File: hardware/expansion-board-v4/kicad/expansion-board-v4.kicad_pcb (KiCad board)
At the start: 6 copper layers, 100 x 62 mm, 176 parts, among them J1 PinHeader_2x20_P2.54mm_Vertic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, J2 U.FL_Hirose_U.FL-R-SMT-1_Vert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, J4 USB_C_Receptacle_HRO_TYPE-C-3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, J5 U.FL_Hirose_U.FL-R-SMT-1_Vert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, J6 U.FL_Hirose_U.FL-R-SMT-1_Vert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, J7 U.FL_Hirose_U.FL-R-SMT-1_Vert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, J8 U.FL_Hirose_U.FL-R-SMT-1_Vert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, J9 MX1.25WT-2P, Q2 SOT-23, Q3 SOT-23, Q4 SOT-23, Q5 SOT-23, SW2 SolderJumper-2_P1.3mm_Open_Pa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, U1 SOT-23-5, U10 QFN-48-1EP_7x7mm_P0.5mm_EP5.1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, U11 DFN-8-1EP_2x2mm_P0.5mm_EP0.86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, U12 SOT-363_SC-70-6, U13 AD8319_LFCSP-8-EP, U14 MSOP-8_3x3mm_P0.65mm, U15 SOT-23-6, U16 SOT-363_SC-70-6, U17 SOT-363_SC-70-6, U18 SOIC-10_3.9x4.9mm_P1mm, U19 QFN-24-1EP_4x4mm_P0.5mm_EP2.6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, U2 SOT-23-5, U20 TSOT-23-6, U3 SOT-23-5, U4 BNO085_LGA-28, U5 BMP388_LGA-10, U6 LGA-16_3x3mm_P0.5mm, U7 ATGM336H_LCC-18, U8 QFN-56-1EP_7x7mm_P0.4mm_EP3.2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, U9 SOIC-8_5.3x5.3mm_P1.27mm, Y1 Crystal_SMD_3225-4Pin_3.2x2.5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, Y2 Crystal_SMD_3225-4Pin_3.2x2.5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, Y3 Crystal_SMD_3215-2Pin_3.2x1.5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

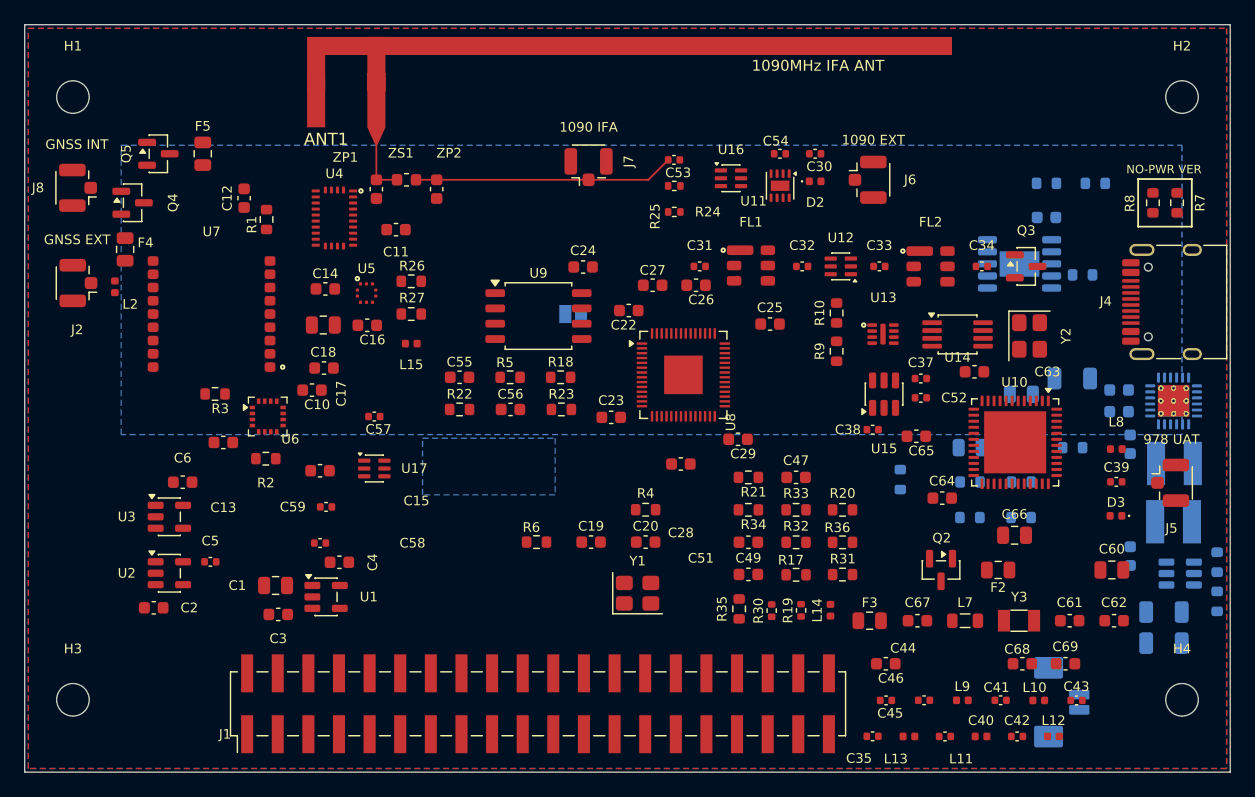
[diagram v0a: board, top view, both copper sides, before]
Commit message: fix(v4): C53 西移 11.6mm，J7→C53 从 14.72 缩到 3.12mm
那 14.72mm 不是设计值。49a61cf 固化时 J7=96.773、C53=103.859，间距 7.09mm；
后来 J7 西移 6.773（评审要求「J7 往西靠」）、C53 东移 1.341 抬上通道，
间距翻倍到 14.720mm——两步操作的副产品，没有任何文档或仿真依据。

J7 是 π 网络之后的 U.FL 抽头，转 90° 让主线水平穿过 pad1，不是 stub；
HFSS 模型只到 ZP1 为止，J7 位置不是电气参数。缩短纯减损耗：
14.72mm 微带 @1090MHz FR4 约 0.15~0.29dB。

C53 → (93.600, 62.865)，撞 J7 courtyard 前的极限（留 0.2mm）。
走廊由 route_ifa_feed.py 自动跟随：23.410 → 11.810mm，腾出 11.6mm 横向通道。
C53 位号撞 J7 位号，用 place_ref.py 重排到本体下方 0.06mm 处。

DRC 0 error、未连接 298、parity 0 均与基线一致；silk_overlap 回到基线 1 条；
5 项走廊测试通过。备份 /tmp/pcb_before_c53west.kicad_pcb。
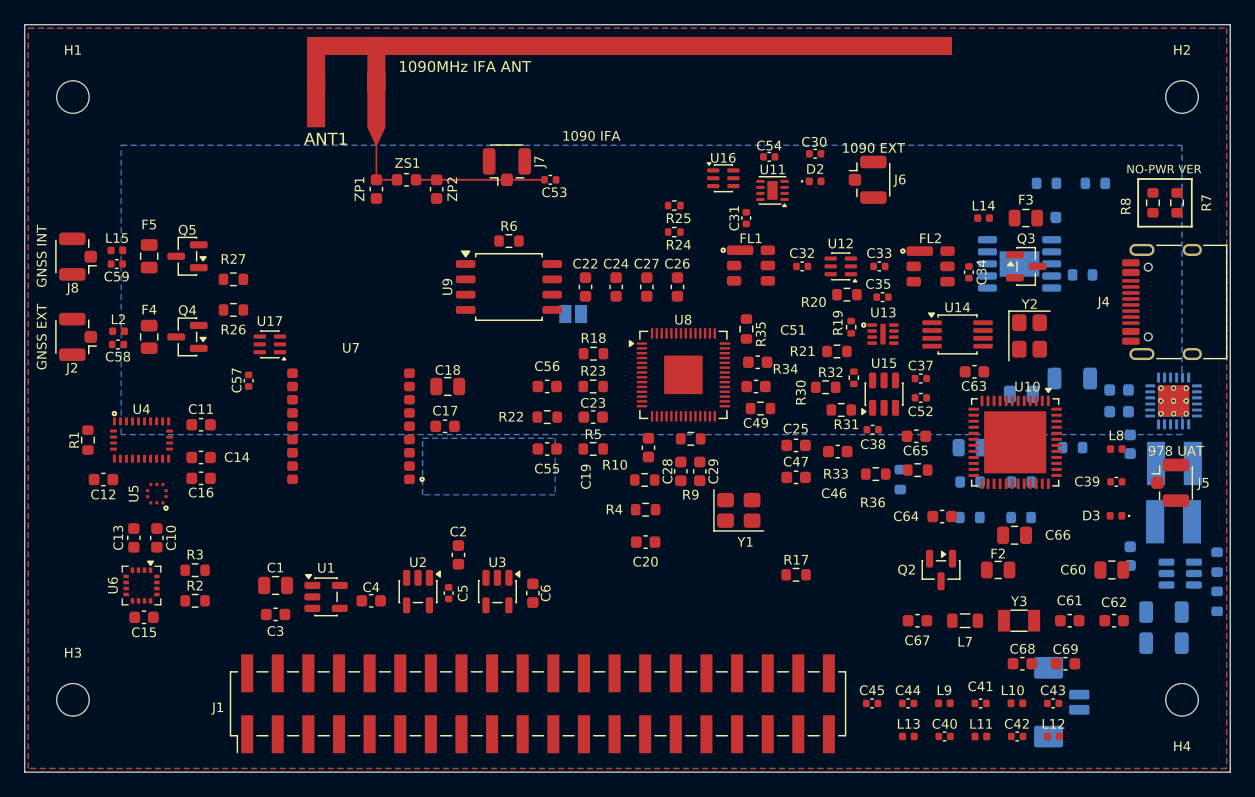
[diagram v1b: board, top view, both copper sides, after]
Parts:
- moved C35 36.4 mm to (121.2, 72.6)
- moved F3 35.8 mm to (133.0, 66.0)
- moved L14 34.9 mm to (129.5, 66.0), turned to 180 degrees
- moved C6 30.5 mm to (92.2, 97.2), turned to 90 degrees
- moved U3 27.9 mm to (89.2, 97.0), turned to -90 degrees
- moved C59 26.6 mm to (57.6, 69.8)
- moved C12 26.1 mm to (56.5, 87.7), turned to 180 degrees
- moved C2 25.7 mm to (86.0, 94.0), turned to 90 degrees
- moved L15 25.6 mm to (57.6, 68.7)
- moved R6 25.1 mm to (90.2, 67.9)
- moved U4 24.4 mm to (59.7, 84.5), turned to 90 degrees
- moved U5 24.1 mm to (61.0, 88.9), turned to -90 degrees
- moved R19 23.9 mm to (118.6, 75.1)
- moved R1 23.5 mm to (55.2, 84.5)
- moved C58 23.5 mm to (57.7, 76.5)
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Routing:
- net IFA_MATCH: track 21.6 -> 10.7 mm

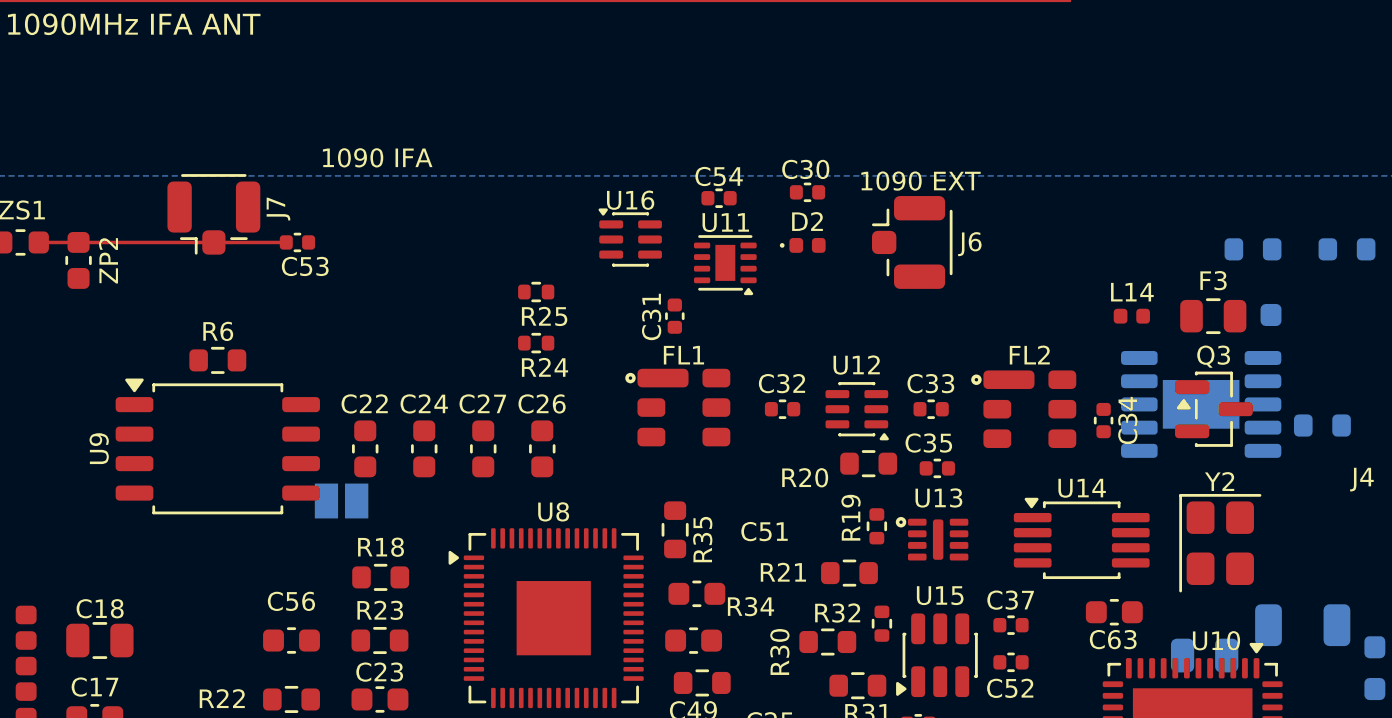
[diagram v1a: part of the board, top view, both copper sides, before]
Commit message: fix(v4): U8 上边四颗去耦退出扇出禁区，并固化 1090 链手工重排
C22/C24/C27/C26 北移 1.057mm（y 71.755 → 70.698）。

依据 apply_keepout.py 的 v3 实测规则：U8 是 QFN-56 7x7 0.4mm pitch，
上边 17 脚(信号 8) → 每圈 10 个过孔 → 需 2 圈 → 净空 0.8+2x0.8 = 2.40mm，
禁区 y 72.473~74.873。这四颗 courtyard 底边在 73.280，踩进去 0.807mm。
北移后底边 72.223，留 0.25mm 余量；越线名单 17 → 15，C26/C27 已移除。

**没有按「往南收到 U8 身边」做**：南边就是扇出禁区本身，SAW 排底边 72.443
与禁区顶边 72.473 之间只有 0.030mm，物理上无解。

同时否掉「搬走这四颗好让 SAW 排西移」：SAW 排西移 Δ 的两端代价
(SAW1_IN + DET_IN) 在 Δ=4.0mm 取最小 7.04mm，而现有余量 2.880mm
已能到 7.17mm——多腾 1.1mm 只换 0.13mm，不划算。

移动后覆铜必须重填：否则 4 颗的 3V3_DIG 焊盘落在旧 GND 铜里，
报 4 条 clearance + 4 条 solder_mask_bridge。重填后 DRC 回到 7 条。

一并固化用户手工重排的 1090 链（U16 转 90°、R24 移到 U16 东侧、
U11/C31/D2/L14/F3/Q3/J6/C30/C54/R19/U13/U14 等 15 件）。
RF50 飞线 255.23 → 247.67mm；SW1_J3 撞 R24 的问题已由该重排消除。
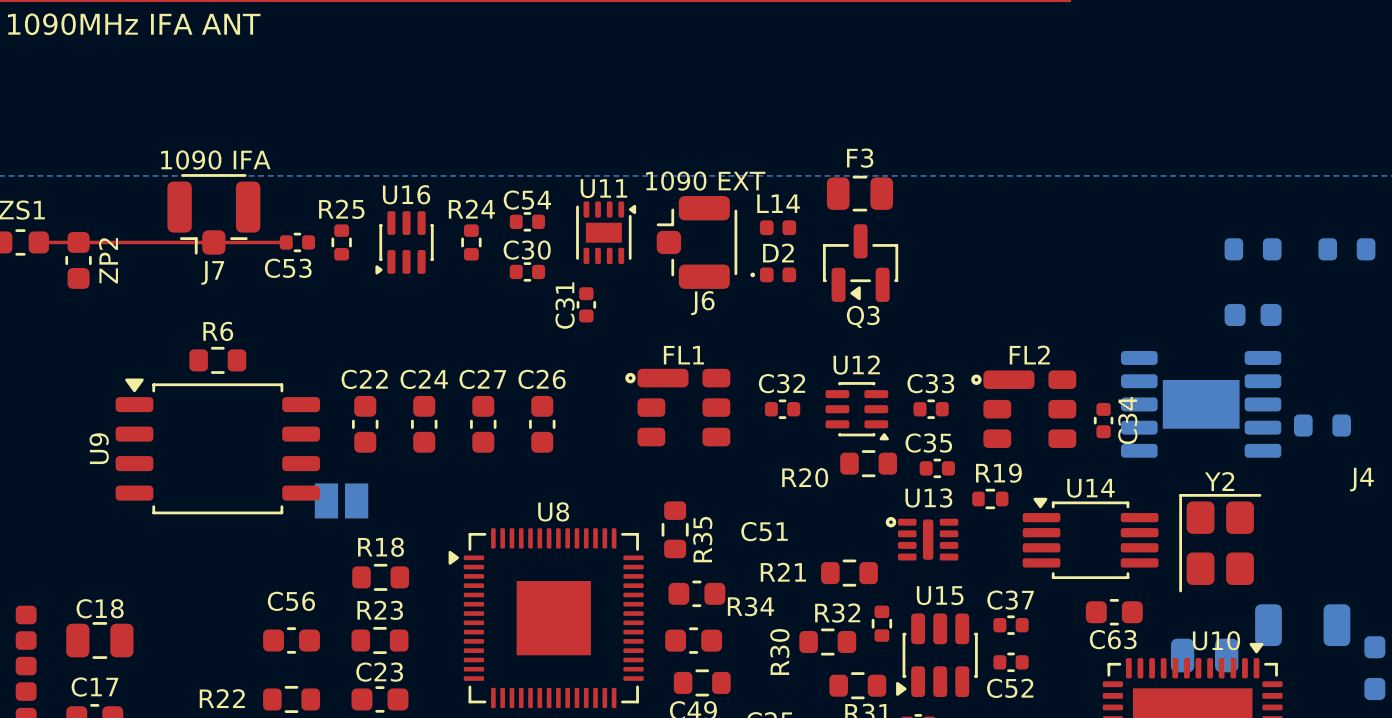
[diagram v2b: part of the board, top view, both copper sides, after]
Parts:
- moved Q3 16.5 mm to (117.9, 63.8), turned to 90 degrees
- moved F3 16.1 mm to (117.8, 60.8)
- moved L14 15.7 mm to (114.3, 62.2)
- moved C30 12.5 mm to (103.5, 64.1), turned to 180 degrees
- moved U16 9.65 mm to (98.3, 62.9), turned to 90 degrees
- moved J6 9.27 mm to (111.1, 62.9)
- moved R25 8.65 mm to (95.5, 62.9), turned to 90 degrees
- moved C54 8.32 mm to (103.5, 62.0)
- moved U11 5.39 mm to (106.8, 62.4), turned to -90 degrees
- moved R24 5.16 mm to (101.1, 62.9), turned to 90 degrees
- moved R19 5.03 mm to (123.4, 73.9), turned to 180 degrees
- moved C31 3.84 mm to (106.0, 65.6)
- moved D2 1.80 mm to (114.3, 64.3)
- moved C27 1.06 mm to (101.6, 70.7)
- moved C26 1.06 mm to (104.1, 70.7)
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
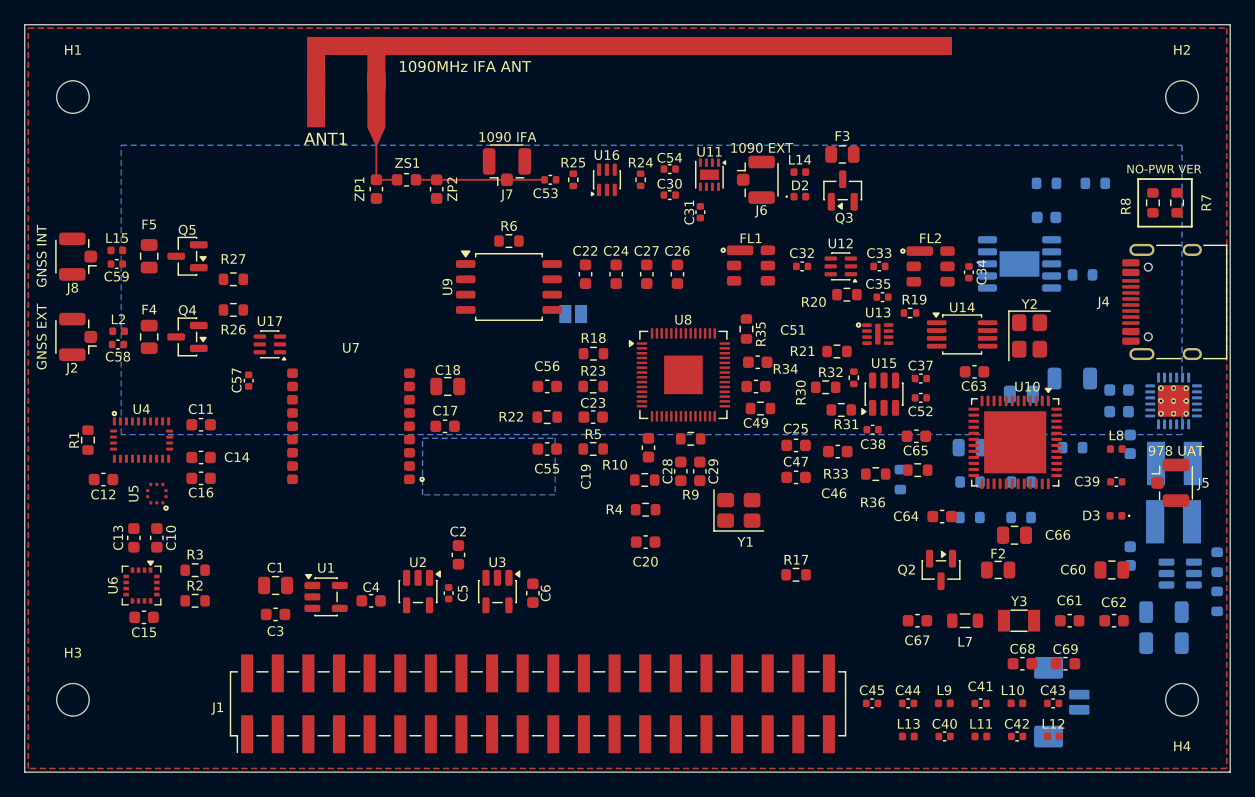
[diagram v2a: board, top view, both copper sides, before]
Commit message: chore(v4): 固化 MCU/Flash 区西移与 1090 前端重排（46 件）
用户手工调整：U8/U9 及其外围整体西移 9.174mm（RP2040 区腾东边空间），
1090 前端 J6 转 90°、U11/C31/D2/L14/Q3/F3/C30/C54 重排。

1090 链验收（对比 6a5a841）：
- ANT1090_EXT J6→C30 穿过 U11 —— 已消除
- ANT1090_EXT 12.05 → 9.92mm，SAW1_IN 4.84 → 2.54mm
- J6→D2（ESD 贴连接器）4.44 → 3.60mm
- U13↔R19 courtyard 重叠已解
- 1090 链飞线总长 87.53 → 87.40mm
- 接收链 C54→U11→C31→FL1→C32→U12→C33→FL2→C34 每跳 dx 均为正（单向东行）

DRC 8 条（0 error）、未连接 298、parity 0、IFA 走廊幂等 + 5 项测试通过。

⚠️ 未解决，投板前必须修：
- J6 ∩ U11 courtyard 重叠 2.590 x 0.302mm。J6 是带金属壳的立式 U.FL，
  U11 是 DFN-8，这是实物打架不是间距警告。解除需 0.502mm。
- U11 位号压自己的 F.Silkscreen 线段。
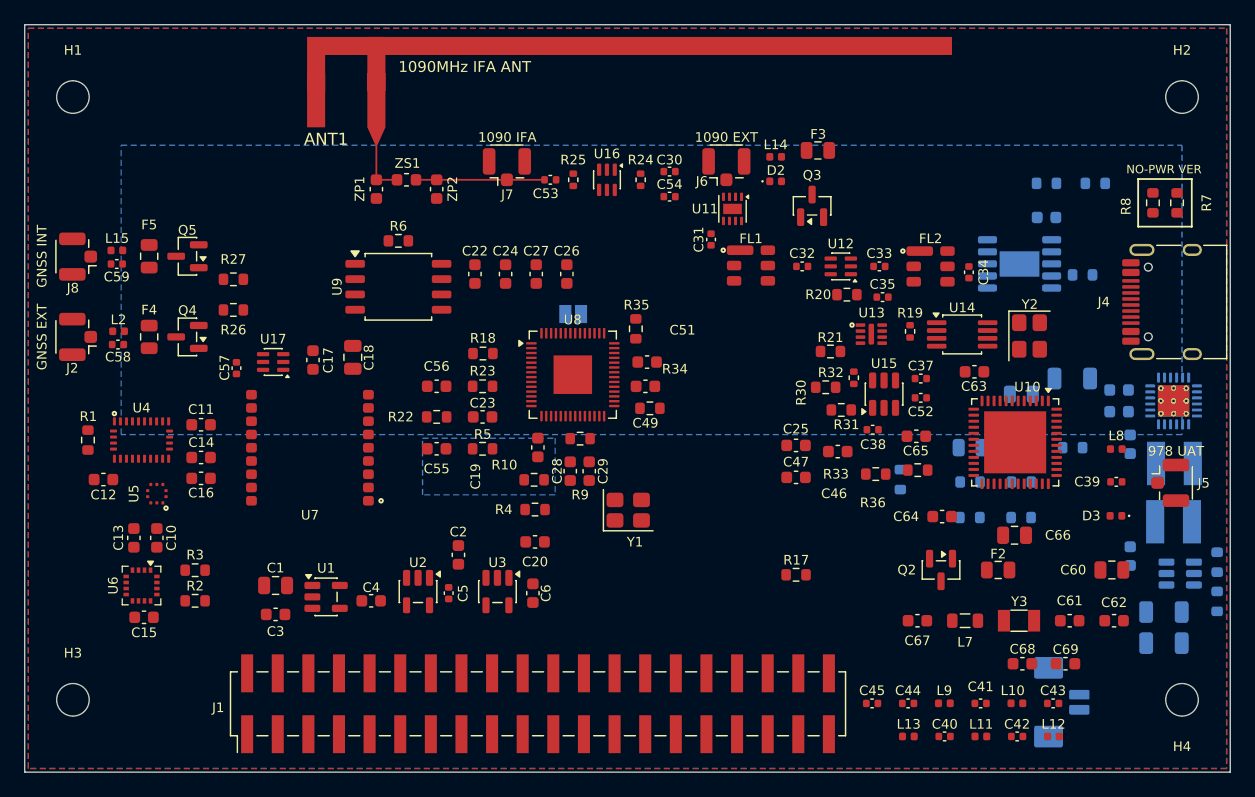
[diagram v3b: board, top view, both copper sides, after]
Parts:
- moved C17 12.3 mm to (73.9, 77.8), turned to -90 degrees
- moved C23 9.17 mm to (88.0, 82.5)
- moved C24 9.17 mm to (89.9, 70.7)
- moved C27 9.17 mm to (92.4, 70.7)
- moved C28 9.17 mm to (95.3, 87.0)
- moved C29 9.17 mm to (96.8, 87.0)
- moved C49 9.17 mm to (101.5, 80.0)
- moved C51 9.17 mm to (101.6, 78.0)
- moved C55 9.17 mm to (84.2, 85.2)
- moved C56 9.17 mm to (84.2, 80.0)
- moved R10 9.17 mm to (92.3, 87.8)
- moved R18 9.17 mm to (88.0, 77.3)
- moved R22 9.17 mm to (84.2, 82.5)
- moved R23 9.17 mm to (88.0, 80.0)
- moved R34 9.17 mm to (101.9, 81.8)
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
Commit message: refactor(v4): U7 南移 + U8/U9 东南移，去耦与晶振组全部归位
评审指出我的方法有硬伤：只在元件当前位置周围找空位，没把芯片本身当成可动的。
空间不是找出来的，是腾出来的。改为刚体位移可行域扫描后：

- 北带净空公式：净空 = U8下移量 - 0.820mm（π 网络 ZP1/ZS1/ZP2 底边 y=65.165
  本来就压在 U8 上边扇出禁区里 0.82mm）
- 扫描发现挡路的是 U7 + C17/C18；U7 组最多南移 4.0mm（再多撞 U1/C1）
- U7 让开后 U8+U9 可走 dx=5/dy=6，北带净空 +5.18mm，够放晶振组（需 ≥4.1mm）

实施：
① U7/C11/C14/C16/C57 南移 4.0mm
② C17/C18 移出 U8 南下路径（C18 再避让 U7 扇出禁区）
③ U8/U9/R6 东南移 (+5.0,+6.0)  —— 刚体同移，QSPI 六条长度完全不变
④ 卫星按「到目标脚最近的可行位」重排，净空规则照抄 apply_keepout.py
   （按信号引脚连续段建禁区，四角可放去耦）

效果：
  3V3_DIG 去耦×6   平均 15.94 → 5.16mm，最远 31.29 → 7.50mm
  RP_1V1 去耦×2    4.89/5.21 → 2.74/3.43mm
  晶振组 Y1/C19/C20/R4  20.5~27.4 → 4.1~8.0mm
  U8 → U15(Slicer) 41.05 → 35.09mm
  QSPI 六条        46.59mm 不变（刚体同移）
  扇出禁区占用      6 → 5（余下 R36/R3/C10/C15/R1 为既存）

DRC 14 条 0 error、未连接 298、parity 0、IFA 走廊幂等 + 5 项测试通过。
余下 silk_overlap 6 条中 4 条是大件位号压自身轮廓（QFN/SOIC 常规做法），
R35↔C55、C51↔R35 两条 silk_over_copper 为既存。

备份 /tmp/pcb_before_bigmove.kicad_pcb
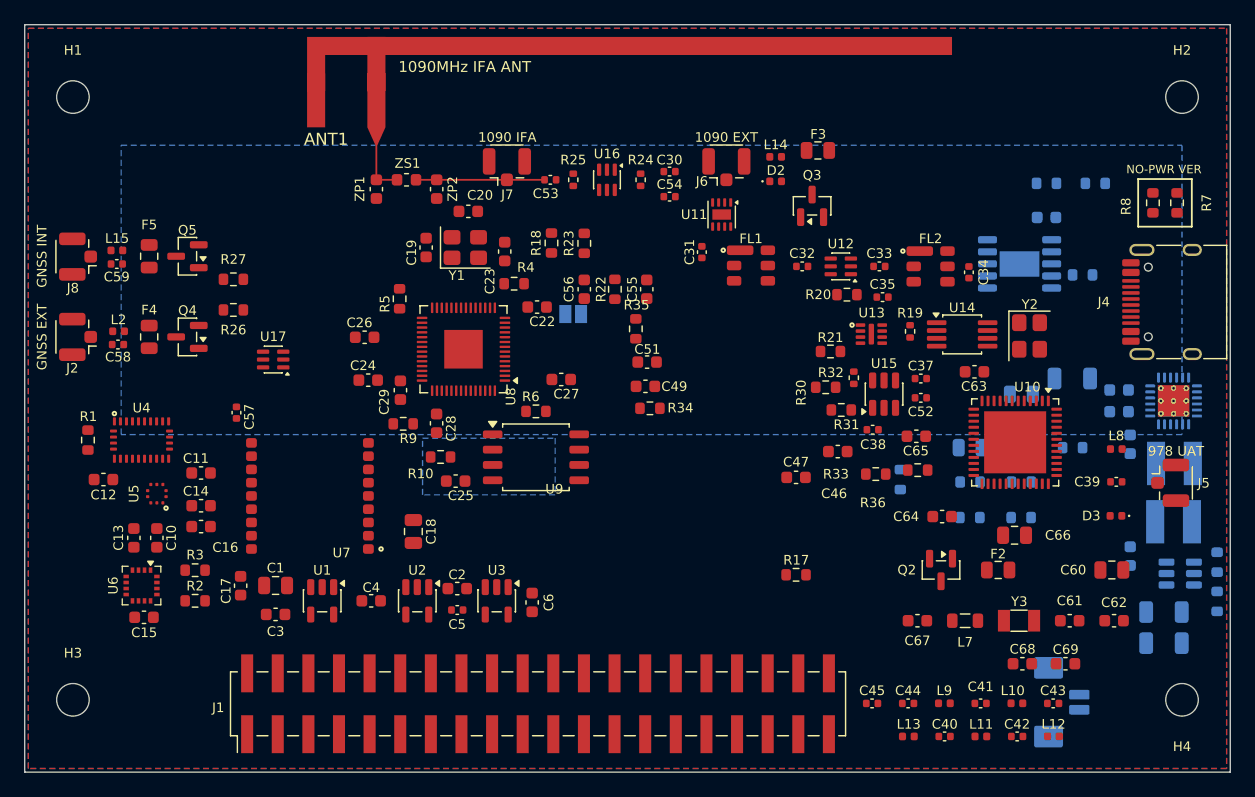
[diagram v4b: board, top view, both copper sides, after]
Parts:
- moved C25 28.4 mm to (85.7, 87.9)
- moved C20 28.0 mm to (86.8, 65.5)
- moved Y1 25.6 mm to (86.5, 68.5)
- moved C55 21.9 mm to (101.6, 71.9), turned to 90 degrees
- moved C17 19.7 mm to (67.9, 96.5)
- moved C19 19.0 mm to (83.3, 68.5)
- moved R4 18.8 mm to (90.6, 71.5)
- moved R22 18.2 mm to (99.0, 71.9), turned to -90 degrees
- moved R6 18.2 mm to (92.4, 82.1)
- moved U9 18.2 mm to (92.4, 85.9)
- moved C26 17.6 mm to (78.2, 75.9), turned to 0 degrees
- moved C29 17.0 mm to (81.2, 80.3)
- moved C18 15.3 mm to (82.2, 92.0)
- moved R9 14.7 mm to (81.4, 83.1)
- moved C56 14.7 mm to (96.4, 71.9), turned to -90 degrees
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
